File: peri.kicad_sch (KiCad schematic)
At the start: 22 parts, among them J10 Conn_02x08_Odd_Even, J11 Conn_01x08, J5 PeriHDR, J6 PI Mating connector, J7 PWR_HDR, Q1 CSD13381F4, Q2 CSD13381F4, SW4 RP8100B2M1CEBLKBLKWHT

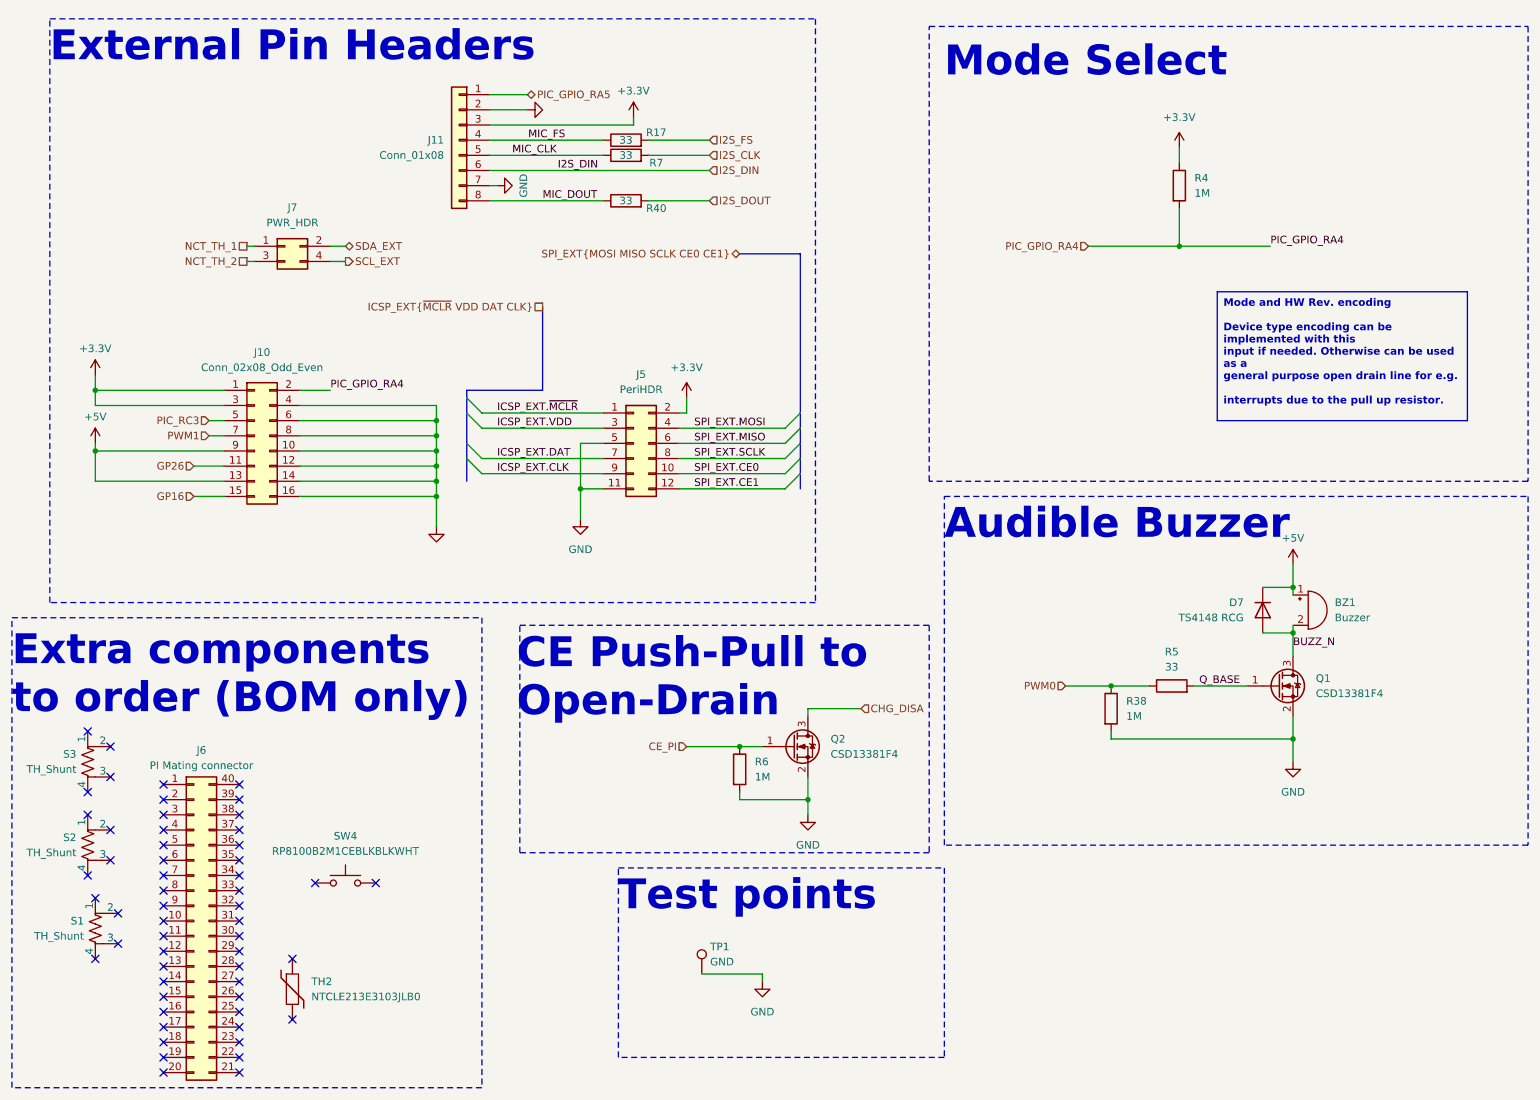
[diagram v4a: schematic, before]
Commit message: feat: 3V3 regulator + complete rework to 16 layers
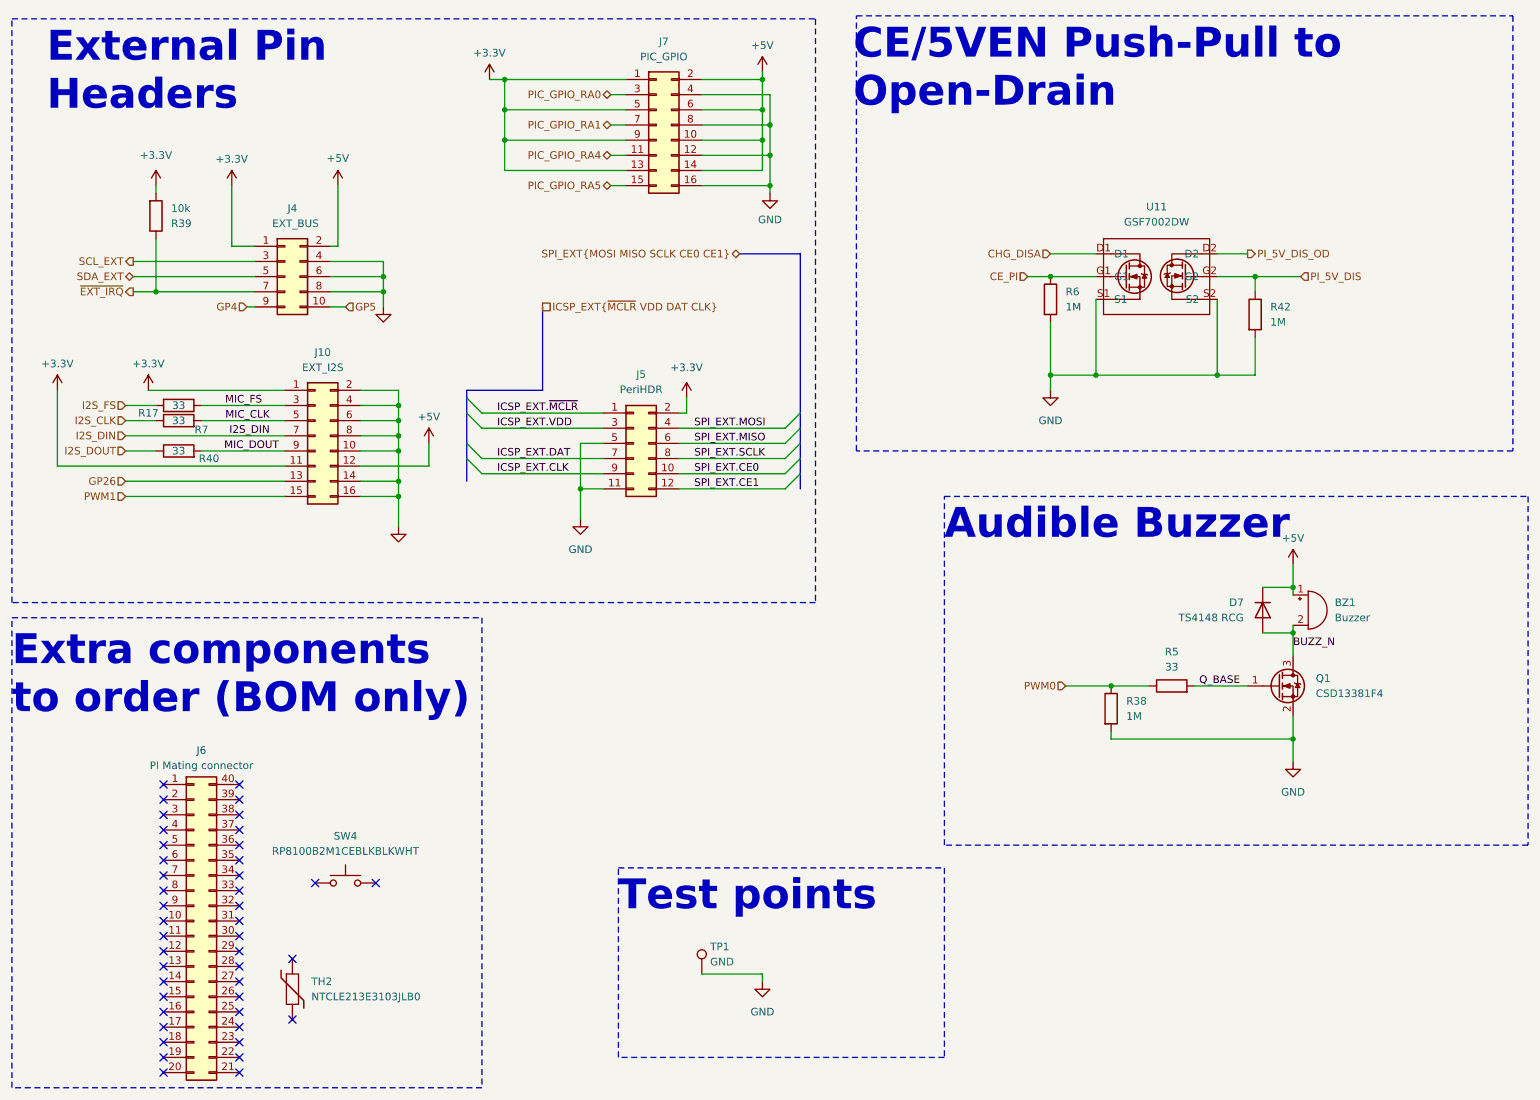
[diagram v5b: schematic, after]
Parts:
- removed J11: Conn_01x08, Connector_PinHeader_2.54mm:PinHeader_1x08_P2.54mm_Vertical, symbol Connector_Generic:Conn_01x08
- removed J7: PWR_HDR, Connector_PinHeader_2.54mm:PinHeader_2x02_P2.54mm_Vertical, symbol Connector_Generic:Conn_02x02_Odd_Even
- removed Q2: CSD13381F4, effectiveRangeHat:YJC0003A_TEX, symbol Transistor_FET:2N7002
- removed R4: 1M, Resistor_SMD:R_0402_1005Metric, symbol Device:R
- removed S1, S2, S3: TH_Shunt, symbol Device:R_Shunt_US
- added J4: EXT_BUS, Connector_PinHeader_2.54mm:PinHeader_2x05_P2.54mm_Vertical, symbol Connector_Generic:Conn_02x05_Odd_Even
- added J7: PIC_GPIO, Connector_PinHeader_2.54mm:PinHeader_2x08_P2.54mm_Vertical, symbol Connector_Generic:Conn_02x08_Odd_Even
- added R39: 10k, Resistor_SMD:R_0402_1005Metric, symbol Device:R
- added R42: 1M, Resistor_SMD:R_0402_1005Metric, symbol Device:R
- added U11: GSF7002DW, effectiveRangeHat:GSF7002DW, symbol effectiveRangeHat_kicad_sym:GSF7002DW
- BZ1: footprint effectiveRangeHat:MagneticBuzzer_CUI_CMT-8504-100-SMT -> effectiveRangeHat:OWMB-505020S-40-12D; MPN CMT-8504-100-SMT-TR -> OWMB-505020S-40-12D; Manufacturer CUI Devices -> Ole Wolff Electronics Inc; SupplierLink https://www.digikey.hu/hu/products/detail/cui-devices/CMT-8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 -> https://www.digikey.com/en/products/detail/ole-wolff-electr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
- J10: value Conn_02x08_Odd_Even -> EXT_I2S
- Q1: footprint effectiveRangeHat:YJC0003A_TEX -> Package_TO_SOT_SMD:SOT-883
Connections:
- net GP16 is gone; now on net PWM1: J10.15 (Pin_15)
- net PIC_RC3 is gone; now on net MIC_CLK: J10.5 (Pin_5)
- net +3.3V: now also J10.11 (Pin_11), J4.1 (Pin_1), J7.1 (Pin_1), J7.13 (Pin_13), J7.5 (Pin_5), J7.9 (Pin_9), R39.2; no longer J10.3 (Pin_3)
- net +5V: now also J10.12 (Pin_12), J4.2 (Pin_2), J7.10 (Pin_10), J7.14 (Pin_14), J7.2 (Pin_2), J7.6 (Pin_6); no longer J10.13 (Pin_13), J10.9 (Pin_9)
- net CE_PI: now also U11.G1
- net CHG_DISA: now also U11.D1
- net GND: now also J10.2 (Pin_2), J4.4 (Pin_4), J4.6 (Pin_6), J4.8 (Pin_8), J7.12 (Pin_12), J7.16 (Pin_16), J7.4 (Pin_4), J7.8 (Pin_8), R42.2, U11.S1, U11.S2; no longer J10.12 (Pin_12)
- net GP26: now also J10.13 (Pin_13); no longer J10.11 (Pin_11)
- net I2S_CLK: now also R7.1; no longer R7.2
- net I2S_DIN: now also J10.7 (Pin_7)
- net I2S_DOUT: now also R40.1; no longer R40.2
- net MIC_CLK: now also R7.2; no longer R7.1
- net MIC_DOUT: now also J10.9 (Pin_9), R40.2; no longer R40.1
- net MIC_FS: now also J10.3 (Pin_3)
- net PIC_GPIO_RA4: now also J7.11 (Pin_11); no longer J10.2 (Pin_2)
- net PIC_GPIO_RA5: now also J7.15 (Pin_15)
- net PWM1: no longer J10.7 (Pin_7)
- net SCL_EXT: now also J4.3 (Pin_3)
- net SDA_EXT: now also J4.5 (Pin_5)
- new net GP4: J4.9 (Pin_9)
- new net GP5: J4.10 (Pin_10)
- new net PIC_GPIO_RA0: J7.3 (Pin_3)
- new net PIC_GPIO_RA1: J7.7 (Pin_7)
- new net PI_5V_DIS: R42.1, U11.G2
- new net PI_5V_DIS_OD: U11.D2
- new net ~{EXT_IRQ}: J4.7 (Pin_7), R39.1
- no-connect marks 56 -> 44
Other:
- note added: "CE/5VEN Push-Pull to Open-Drain"
- note removed: "CE Push-Pull to Open-Drain"
- note removed: "Mode Select"
- moved on the sheet: J10, R17, R40, R6, R7
